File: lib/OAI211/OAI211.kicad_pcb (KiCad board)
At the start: 2 copper layers, 8 parts

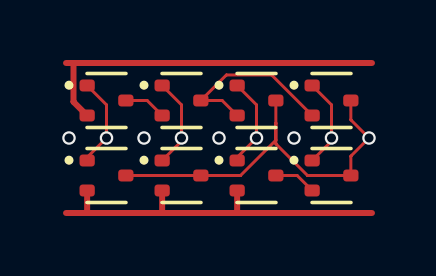
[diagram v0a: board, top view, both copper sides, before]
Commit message: High-density layout with pitch of 1.1mm, which gains 23% !!
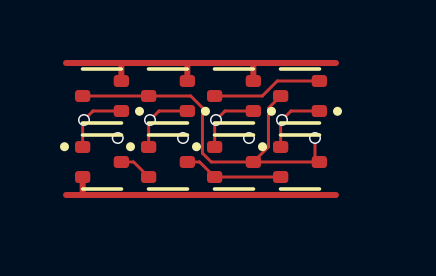
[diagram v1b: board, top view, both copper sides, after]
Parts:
- moved N4 1.14 mm to (7.70, 3.30)
- moved P4 1.06 mm to (7.70, 1.10), turned to 180 degrees
- moved N3 0.87 mm to (5.50, 3.30)
- moved P3 0.76 mm to (5.50, 1.10), turned to 180 degrees
- moved N2 0.64 mm to (3.30, 3.30)
- moved N1 0.47 mm to (1.10, 3.30)
- moved P2 0.47 mm to (3.30, 1.10), turned to 180 degrees
- moved P1 0.21 mm to (1.10, 1.10), turned to 180 degrees
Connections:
- N1 pad 3: Y -> intNA
- N2 pad 2: GND -> intNA
- N2 pad 3: Y -> intNB
- N3 pad 2: GND -> intNB
- N3 pad 3: intC -> Y
- N4 pad 2: intC -> intNB
- P1 pad 3: intPA -> Y
- P2 pad 2: intPA -> VDD
- P2 pad 3: intPB -> Y
- P3 pad 2: intPB -> VDD
- P3 pad 3: Y -> intC
- P4 pad 2: intPB -> intC
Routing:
- net intPB: track 6.04 -> 0.00 mm
- net intNB: track 0.00 -> 3.32 mm
- net GND: track 12.5 -> 9.61 mm
- net intC: track 1.42 -> 3.70 mm
- net intPA: track 1.42 -> 0.00 mm
- net VDD: track 12.1 -> 10.8 mm
- net intNA: track 0.00 -> 1.12 mm
- net C1: track 3.03 -> 2.29 mm
- net B: track 3.03 -> 2.29 mm
- net A: track 3.03 -> 2.29 mm
- net C2: track 3.03 -> 2.29 mm
- net (no net): vias 4 -> 3
